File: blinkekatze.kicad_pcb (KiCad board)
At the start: 4 copper layers, 68.1 x 69 mm, 109 parts, among them J1 Power key, J2 Conn_01x06, Q1 AO3400A, Q2 AO3400A, U1 ESP32-C3-MINI-1, U2 BQ27546, U3 SRV05-4, U4 FM2113, U5 SPL06-001, U7 LTR-303ALS-01, U8 BQ24295, U9 TPS63001

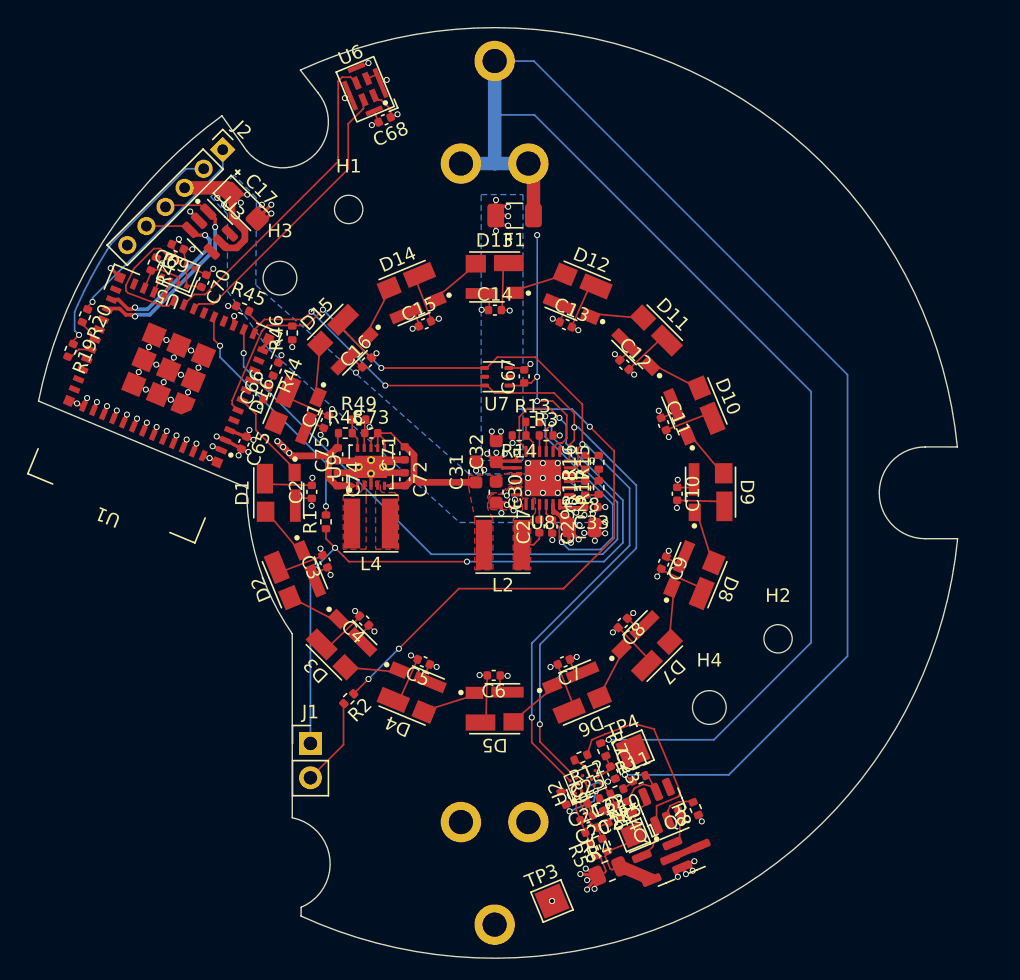
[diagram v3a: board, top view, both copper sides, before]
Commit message: Hide silkscreen designators
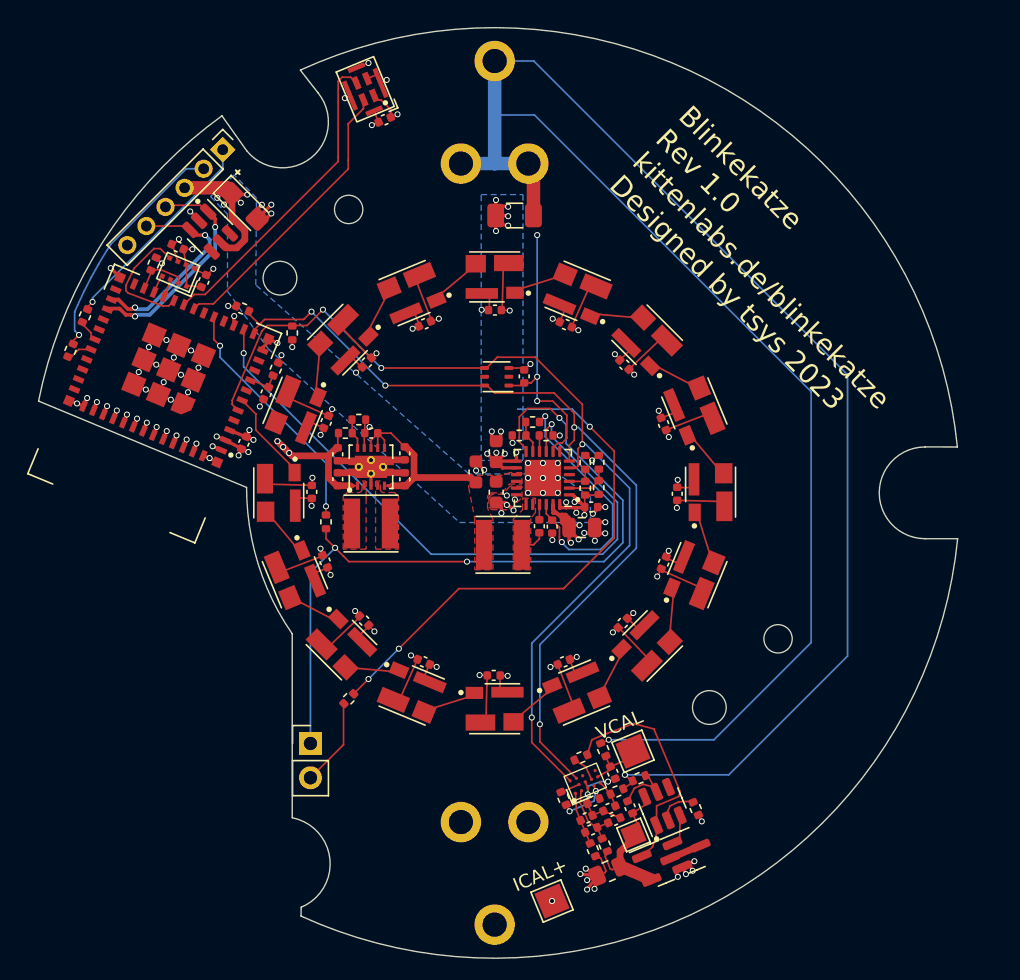
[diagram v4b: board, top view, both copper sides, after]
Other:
- board text added: "Blinkekatze Rev 1.0 kittenlabs.de/blinkekatze Designed by tsys 2023"
- board text added: "D+"
- board text added: "D-"
- board text added: "GND"
- board text added: "ICAL+"
- board text added: "LED1"
- board text added: "LED2"
- board text added: "PWR_ON"
- board text added: "VBAT"
- board text added: "VBUS"
- board text added: "VCAL"

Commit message: JLCPCB DFM
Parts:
- added H5: Tooling hole, ToolingHole:ToolingHole_JLCSMT, F.Cu at (89.0, 130.5)
- added H6: Tooling hole, ToolingHole:ToolingHole_JLCSMT, F.Cu at (110.5, 69.5)
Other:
- board text added: "JLCJLCJLCJLC"
- board text added: "Kittenlabs Blinkekatze Rev 1.0 kittenlabs.de/blinkekatze Designed by tsys in 2023"
- board text removed: "Blinkekatze Rev 1.0 kittenlabs.de/blinkekatze Designed by tsys 2023"

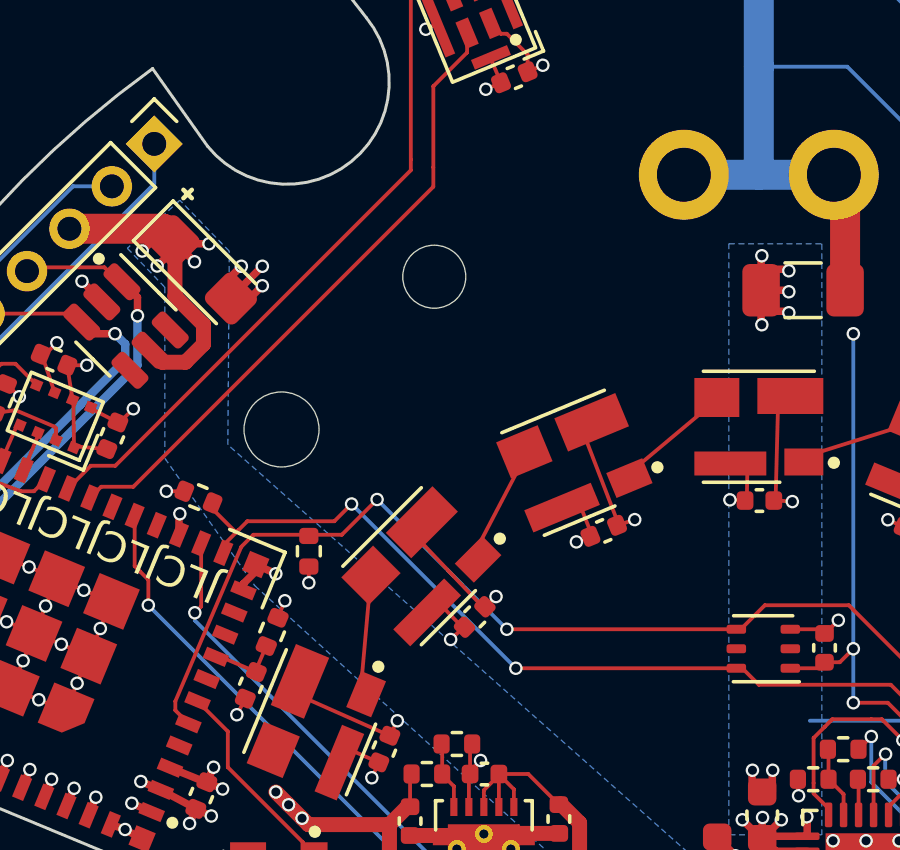
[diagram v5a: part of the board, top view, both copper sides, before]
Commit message: Add accelerometer
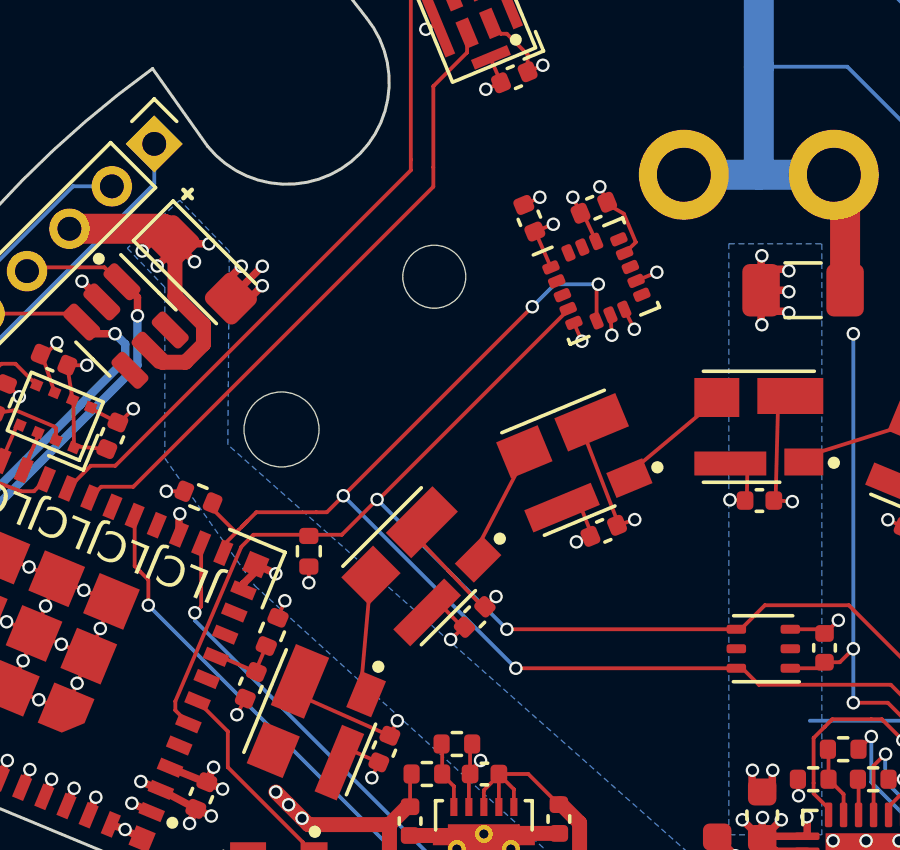
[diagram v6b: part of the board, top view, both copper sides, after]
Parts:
- added C18: 1uF, Capacitor_SMD:C_0402_1005Metric, F.Cu at (92.3, 77.0)
- added C19: 1uF, Capacitor_SMD:C_0402_1005Metric, F.Cu at (94.5, 76.7)
- added U10: LIS3DH, Package_LGA:LGA-16_3x3mm_P0.5mm_LayoutBorder3x5y, F.Cu at (94.6, 79.1)
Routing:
- net /Battery/SDA: track 64.9 -> 78.1 mm, vias 4 -> 6
- net /Battery/SCL: track 70.4 -> 79.4 mm
- net GND: track 119.0 -> 124.5 mm, vias 94 -> 99
- net +3V3: track 43.1 -> 47.5 mm, vias 15 -> 18
